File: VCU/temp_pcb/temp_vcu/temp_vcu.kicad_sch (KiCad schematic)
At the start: 28 parts, among them J1 39-30-1080, J2 39-30-1120, U2 NUCLEO-F429ZI

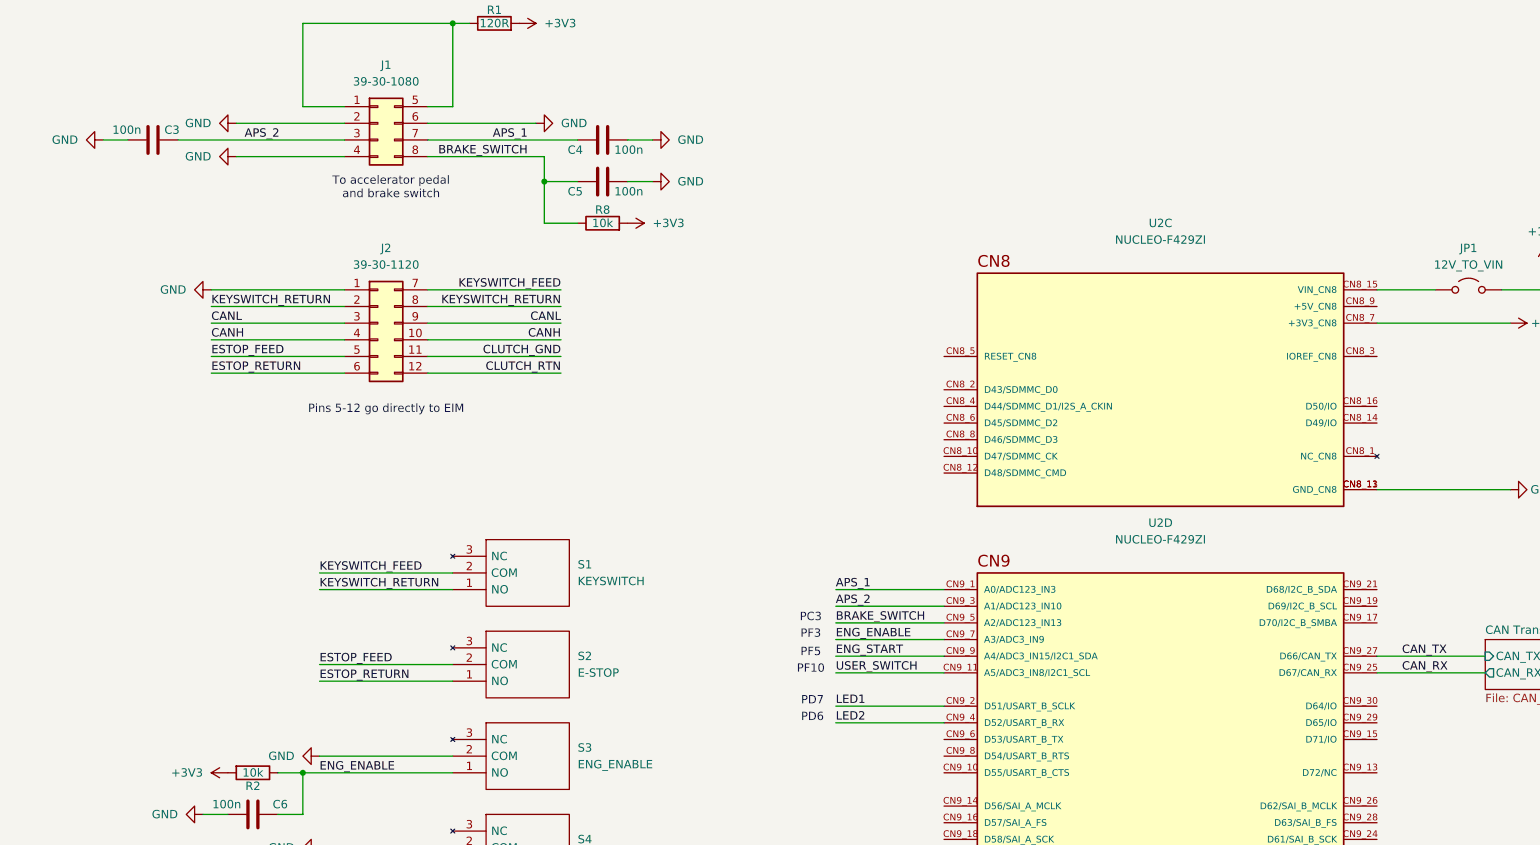
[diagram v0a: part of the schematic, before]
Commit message: Ordered version of board
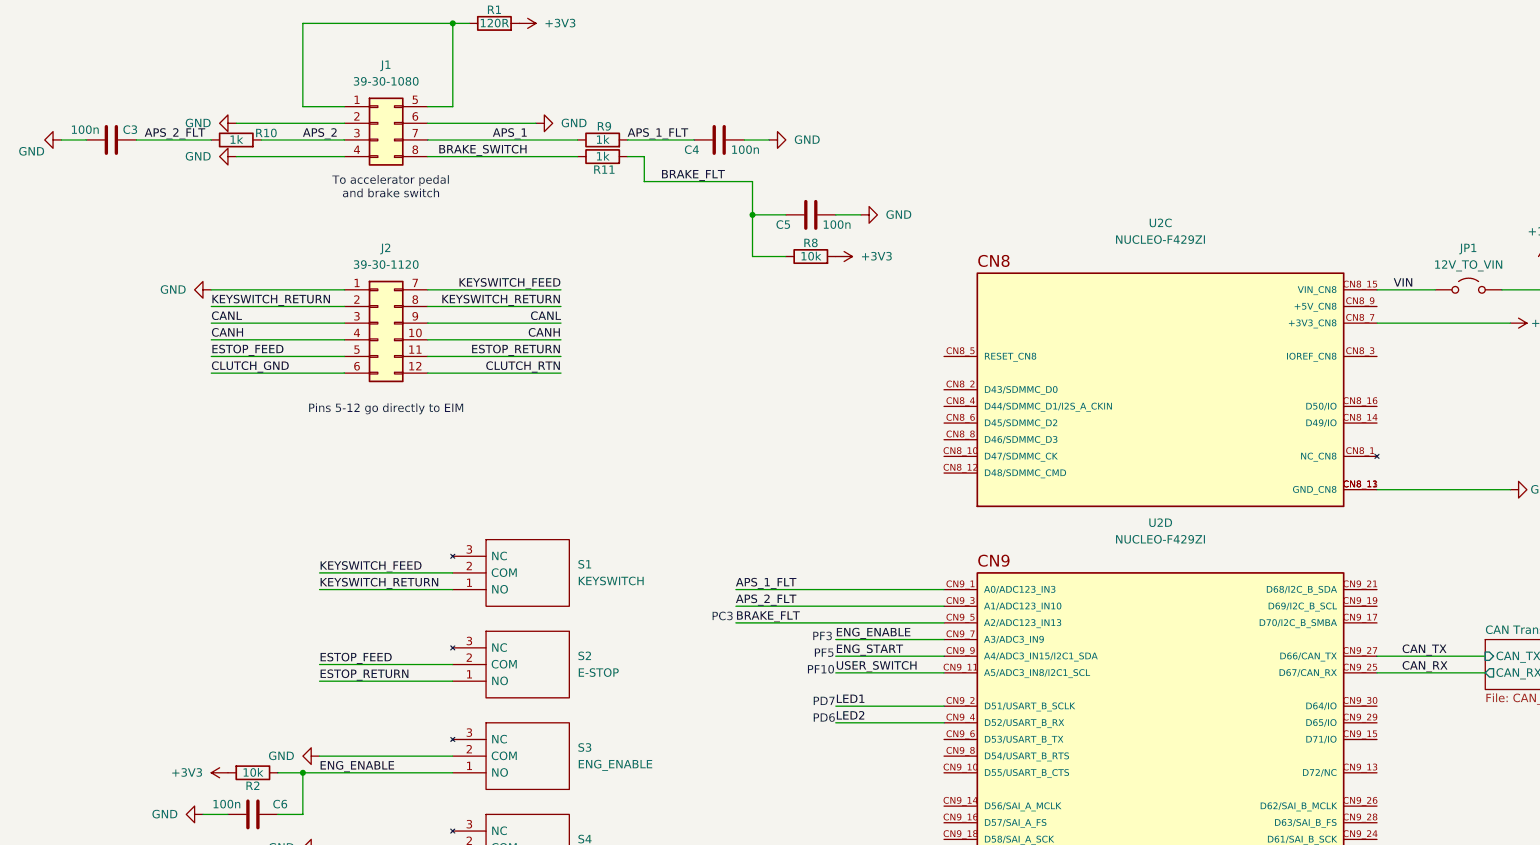
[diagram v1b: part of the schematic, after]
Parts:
- added R10, R11, R9: 1k, Resistor_THT:R_Axial_DIN0207_L6.3mm_D2.5mm_P10.16mm_Horizontal, symbol Device:R
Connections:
- net APS_1: now also R9.1; no longer C4.2, U2.CN9_1 (A0/ADC123_IN3)
- net APS_2: now also R10.2; no longer C3.2, U2.CN9_3 (A1/ADC123_IN10)
- net BRAKE_SWITCH: now also R11.1; no longer C5.2, R8.1, U2.CN9_5 (A2/ADC123_IN13)
- net CLUTCH_GND: now also J2.6 (Pin_6); no longer J2.11 (Pin_11)
- net ESTOP_RETURN: now also J2.11 (Pin_11); no longer J2.6 (Pin_6)
- net VIN: now reaches JP1.1 (A), U2.CN8_15 (VIN_CN8)
- new net APS_1_FLT: C4.2, R9.2, U2.CN9_1 (A0/ADC123_IN3)
- new net APS_2_FLT: C3.2, R10.1, U2.CN9_3 (A1/ADC123_IN10)
- new net BRAKE_FLT: C5.2, R11.2, R8.1, U2.CN9_5 (A2/ADC123_IN13)
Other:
- moved on the sheet: C3, C4, C5, R8
